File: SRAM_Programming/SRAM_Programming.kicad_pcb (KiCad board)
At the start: 2 copper layers, 2 parts, among them U1 IS62C256AL

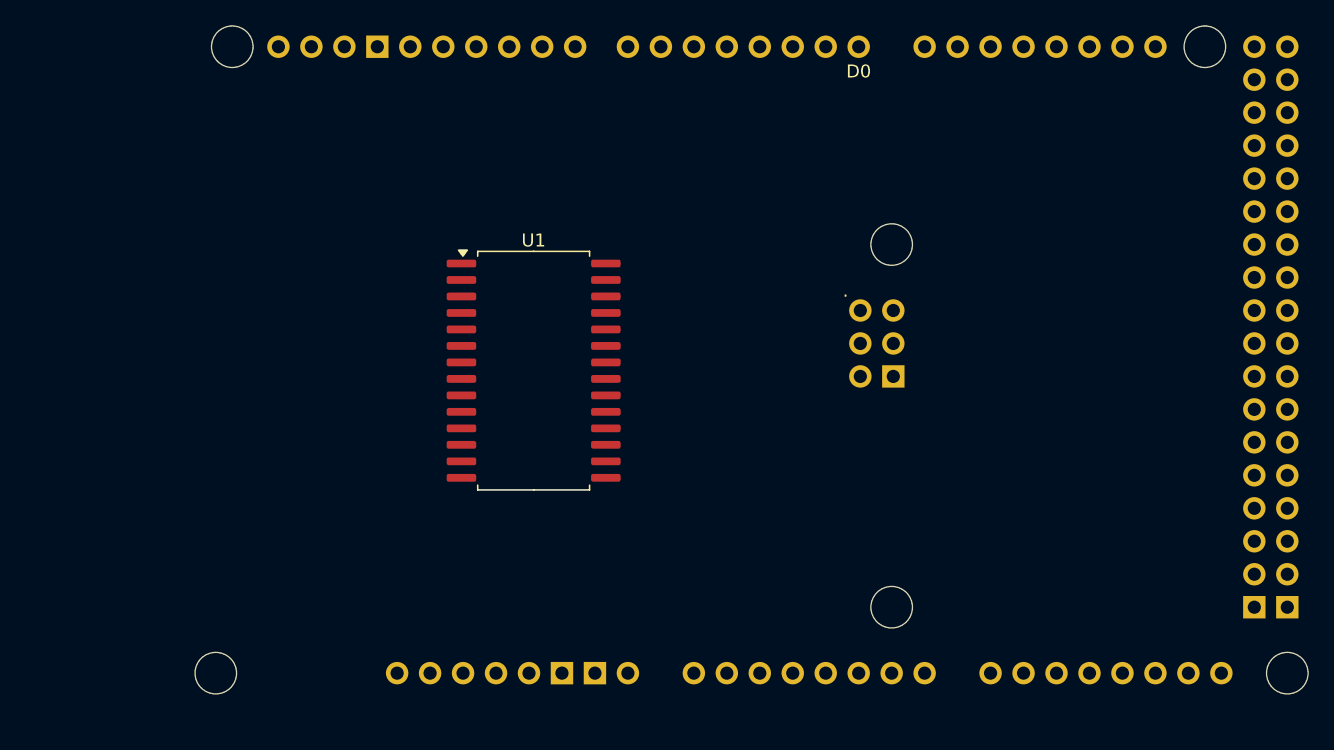
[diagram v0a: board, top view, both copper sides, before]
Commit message: started pcb layout
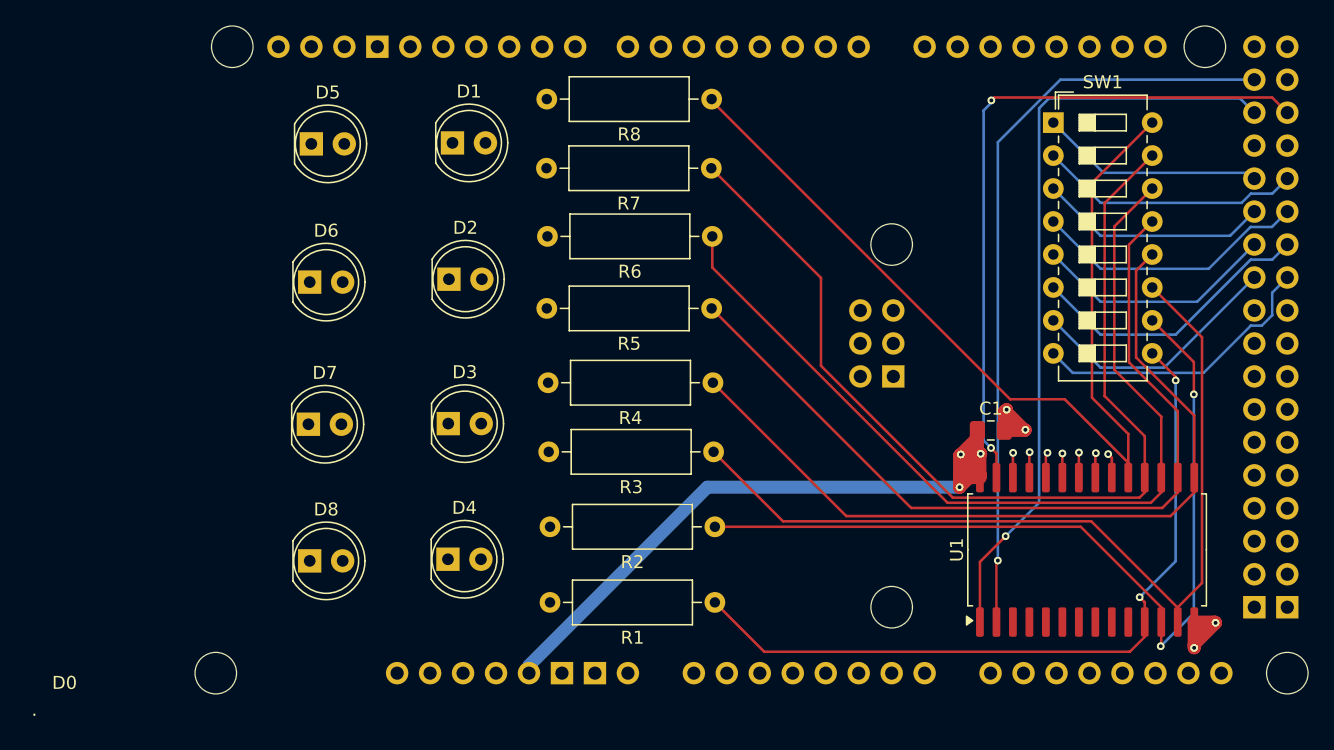
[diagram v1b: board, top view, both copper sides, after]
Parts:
- added C1: 0.01u, Capacitor_SMD:C_0805_2012Metric_Pad1.18x1.45mm_HandSolder, F.Cu at (132.8, 82.2)
- added D1: LED, LED_THT:LED_D5.0mm, F.Cu at (91.3, 60.0)
- added D2: LED, LED_THT:LED_D5.0mm, F.Cu at (91.1, 70.5)
- added D3: LED, LED_THT:LED_D5.0mm, F.Cu at (91.0, 81.7)
- added D4: LED, LED_THT:LED_D5.0mm, F.Cu at (91.0, 92.1)
- added D5: LED, LED_THT:LED_D5.0mm, F.Cu at (80.5, 60.1)
- added D6: LED, LED_THT:LED_D5.0mm, F.Cu at (80.3, 70.8)
- added D7: LED, LED_THT:LED_D5.0mm, F.Cu at (80.2, 81.7)
- added D8: LED, LED_THT:LED_D5.0mm, F.Cu at (80.3, 92.2)
- added R1: R, Resistor_THT:R_Axial_DIN0309_L9.0mm_D3.2mm_P12.70mm_Horizontal, F.Cu at (111.5, 95.5)
- added R2: R, Resistor_THT:R_Axial_DIN0309_L9.0mm_D3.2mm_P12.70mm_Horizontal, F.Cu at (111.5, 89.6)
- added R3: R, Resistor_THT:R_Axial_DIN0309_L9.0mm_D3.2mm_P12.70mm_Horizontal, F.Cu at (111.5, 83.8)
- added R4: R, Resistor_THT:R_Axial_DIN0309_L9.0mm_D3.2mm_P12.70mm_Horizontal, F.Cu at (111.4, 78.5)
- added R5: R, Resistor_THT:R_Axial_DIN0309_L9.0mm_D3.2mm_P12.70mm_Horizontal, F.Cu at (111.3, 72.8)
- added R6: R, Resistor_THT:R_Axial_DIN0309_L9.0mm_D3.2mm_P12.70mm_Horizontal, F.Cu at (111.3, 67.2)
- added R7: R, Resistor_THT:R_Axial_DIN0309_L9.0mm_D3.2mm_P12.70mm_Horizontal, F.Cu at (111.3, 62.0)
- added R8: R, Resistor_THT:R_Axial_DIN0309_L9.0mm_D3.2mm_P12.70mm_Horizontal, F.Cu at (111.3, 56.7)
- added SW1: SW_DIP_x08, Button_Switch_THT:SW_DIP_SPSTx08_Slide_6.7x21.88mm_W7.62mm_P2.54mm_LowProfile, F.Cu at (137.6, 58.5)
- moved U1 44.8 mm to (140.2, 91.4), turned to 90 degrees
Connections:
- A1 pad D28: Net-(U1-I/O7) -> Net-(A1-PadD28)
- A1 pad D29: Net-(U1-I/O6) -> Net-(A1-PadD29)
- A1 pad D30: Net-(U1-I/O5) -> Net-(A1-PadD30)
- A1 pad D31: Net-(U1-I/O4) -> Net-(A1-PadD31)
- A1 pad D32: Net-(U1-I/O3) -> Net-(A1-PadD32)
- A1 pad D33: Net-(U1-I/O2) -> Net-(A1-PadD33)
- A1 pad D34: Net-(U1-I/O1) -> Net-(A1-PadD34)
- A1 pad D35: Net-(U1-I/O0) -> Net-(A1-PadD35)
- A1 pad GND2: unconnected-(A1-GND-PadGND2) -> GND
- A1 pad GND3: unconnected-(A1-GND-PadGND3) -> GND
- A1 pad GND5: unconnected-(A1-GND-PadGND5) -> GND
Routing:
- net Net-(U1-I/O6): track 0.00 -> 76.8 mm
- net Net-(U1-I/O7): track 0.00 -> 75.4 mm
- net Net-(U1-I/O5): track 0.00 -> 70.9 mm
- net Net-(U1-I/O2): track 0.00 -> 70.0 mm
- net Net-(U1-I/O1): track 0.00 -> 67.5 mm, vias 0 -> 2
- net Net-(U1-I/O4): track 0.00 -> 65.9 mm
- net Net-(U1-I/O3): track 0.00 -> 62.8 mm
- net Net-(U1-I/O0): track 0.00 -> 59.1 mm, vias 0 -> 2
- net Net-(U1-A14): track 0.00 -> 58.8 mm, vias 0 -> 1
- net Net-(U1-A12): track 0.00 -> 58.8 mm, vias 0 -> 1
- net +5V: track 0.00 -> 57.2 mm, vias 0 -> 3
- net Net-(U1-~{WE}): track 0.00 -> 53.1 mm, vias 0 -> 2
- net Net-(A1-PadD35): track 0.00 -> 22.7 mm
- net Net-(A1-PadD33): track 0.00 -> 22.4 mm
- net Net-(A1-PadD31): track 0.00 -> 21.4 mm
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
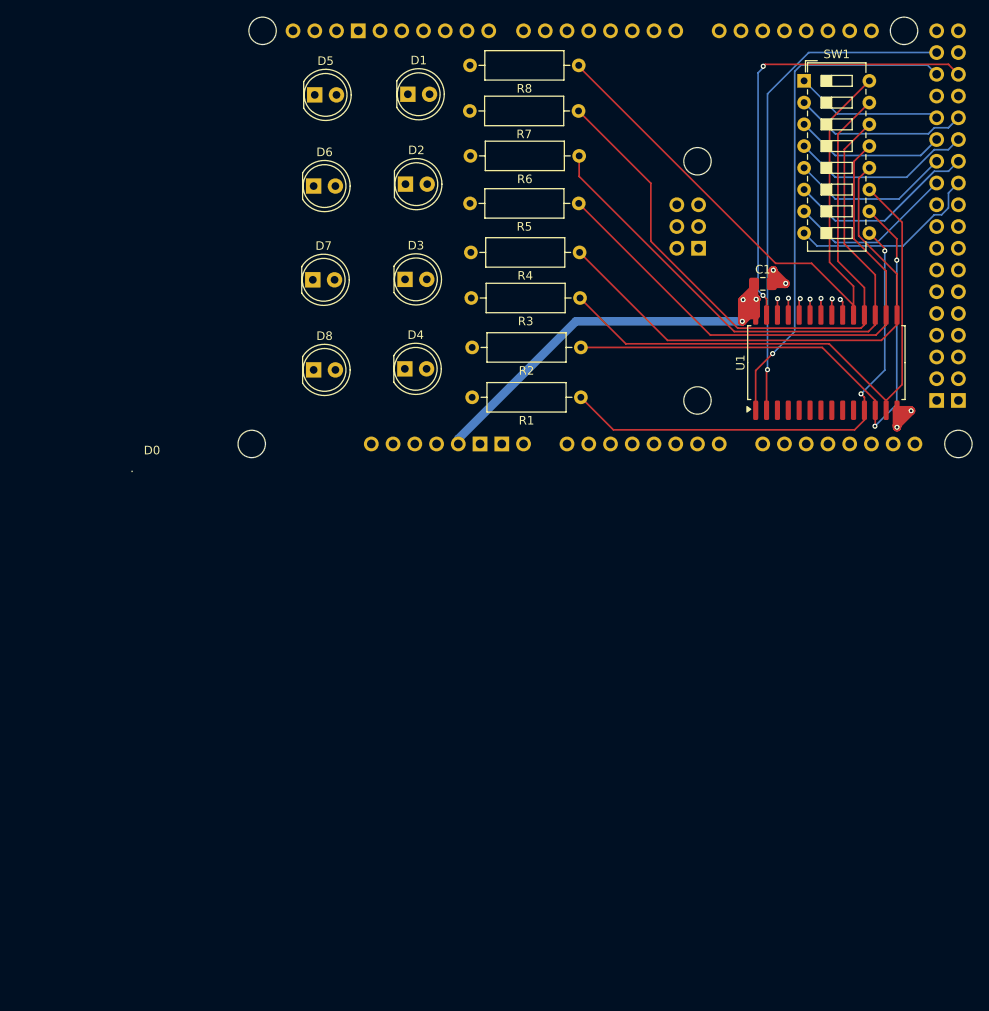
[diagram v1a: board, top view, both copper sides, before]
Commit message: Finish first version of sram shield
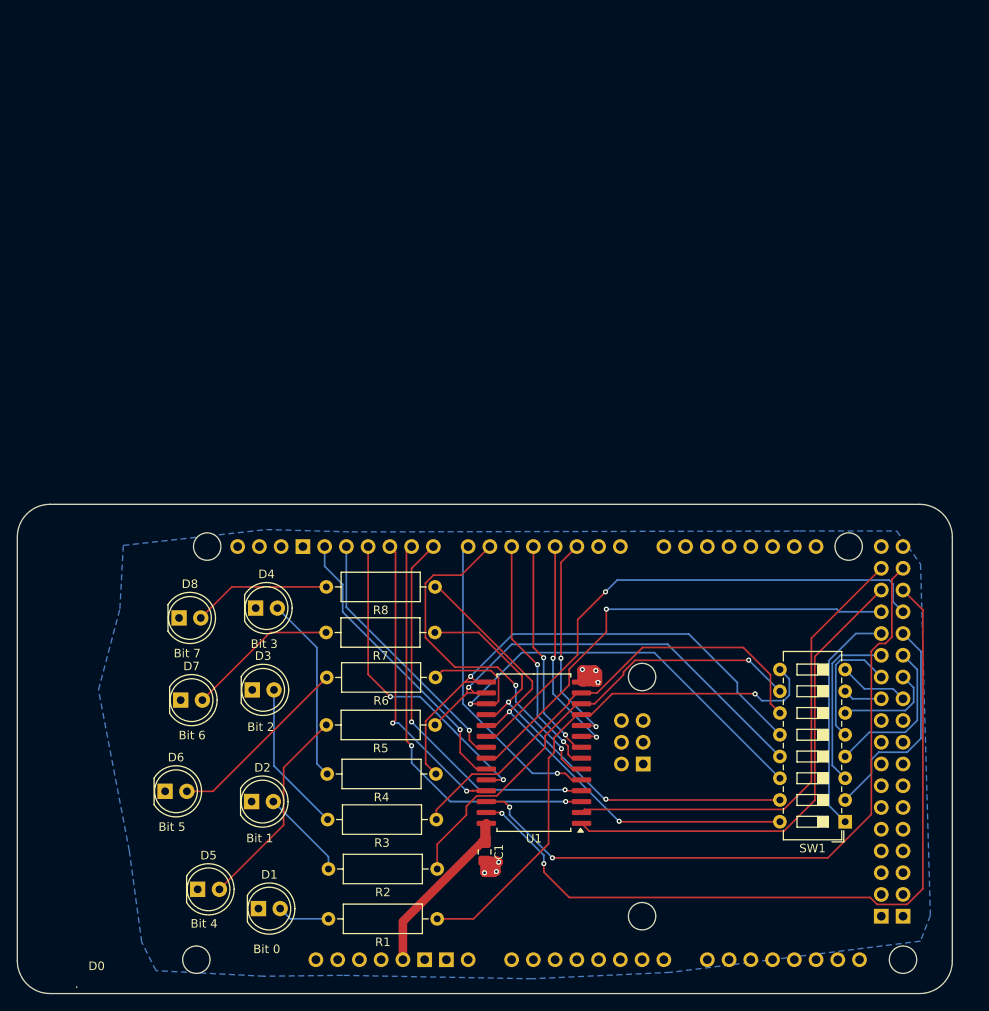
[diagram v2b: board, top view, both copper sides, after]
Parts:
- moved D1 96.7 mm to (73.9, 155.2)
- moved D5 93.8 mm to (66.8, 152.9)
- moved SW1 86.7 mm to (142.4, 145.0), turned to 180 degrees
- moved D2 74.3 mm to (73.1, 142.7)
- moved C1 73.9 mm to (100.3, 148.6), turned to -90 degrees
- moved D6 72.8 mm to (63.0, 141.5)
- moved R2 63.2 mm to (94.8, 150.6)
- moved R3 63.2 mm to (94.7, 144.8)
- moved R6 63.2 mm to (94.6, 128.2)
- moved R1 63.2 mm to (94.8, 156.4)
- moved R5 63.2 mm to (94.5, 133.7)
- moved R7 63.2 mm to (94.5, 122.9)
- moved R8 63.2 mm to (94.5, 117.6)
- moved R4 63.2 mm to (94.6, 139.4)
- moved A1 60.6 mm to (52.7, 163.7)
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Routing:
- net Net-(U1-A13): track 1.92 -> 81.1 mm, vias 1 -> 2
- net Net-(U1-~{CE}): track 1.93 -> 61.4 mm
- net Net-(U1-~{OE}): track 1.94 -> 56.1 mm
- net Net-(U1-A7): track 0.00 -> 47.5 mm, vias 0 -> 2
- net Net-(U1-A6): track 0.00 -> 44.7 mm, vias 0 -> 2
- net Net-(U1-A4): track 0.00 -> 42.1 mm, vias 0 -> 2
- net Net-(U1-~{WE}): track 53.1 -> 93.2 mm
- net Net-(U1-A5): track 0.00 -> 36.2 mm, vias 0 -> 1
- net Net-(U1-A9): track 1.96 -> 37.9 mm, vias 1 -> 2
- net +5V: track 57.2 -> 22.3 mm, vias 3 -> 0
- net Net-(U1-A8): track 1.97 -> 35.3 mm, vias 1 -> 2
- net Net-(U1-A11): track 1.86 -> 34.5 mm
- net Net-(U1-A10): track 1.90 -> 30.9 mm
- net Net-(U1-A3): track 0.00 -> 28.8 mm, vias 0 -> 2
- net Net-(A1-D3_INT1): track 0.00 -> 26.3 mm, vias 0 -> 2
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- added copper zone on B.Cu, net GND
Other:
- board outline added: 109.2 x 57.1 mm
- board text added: "Bit 0"
- board text added: "Bit 1"
- board text added: "Bit 2"
- board text added: "Bit 3"
- board text added: "Bit 4"
- board text added: "Bit 5"
- board text added: "Bit 6"
- board text added: "Bit 7"
